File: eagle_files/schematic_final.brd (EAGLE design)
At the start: 77.9 x 100 mm, 46 parts, among them IC1 IC_ULN2003-TSSOP-16, T1 BPX81, T2 BPX81, T3 BPX81, T4 BPX81, T5 BPX81, T6 BPX81

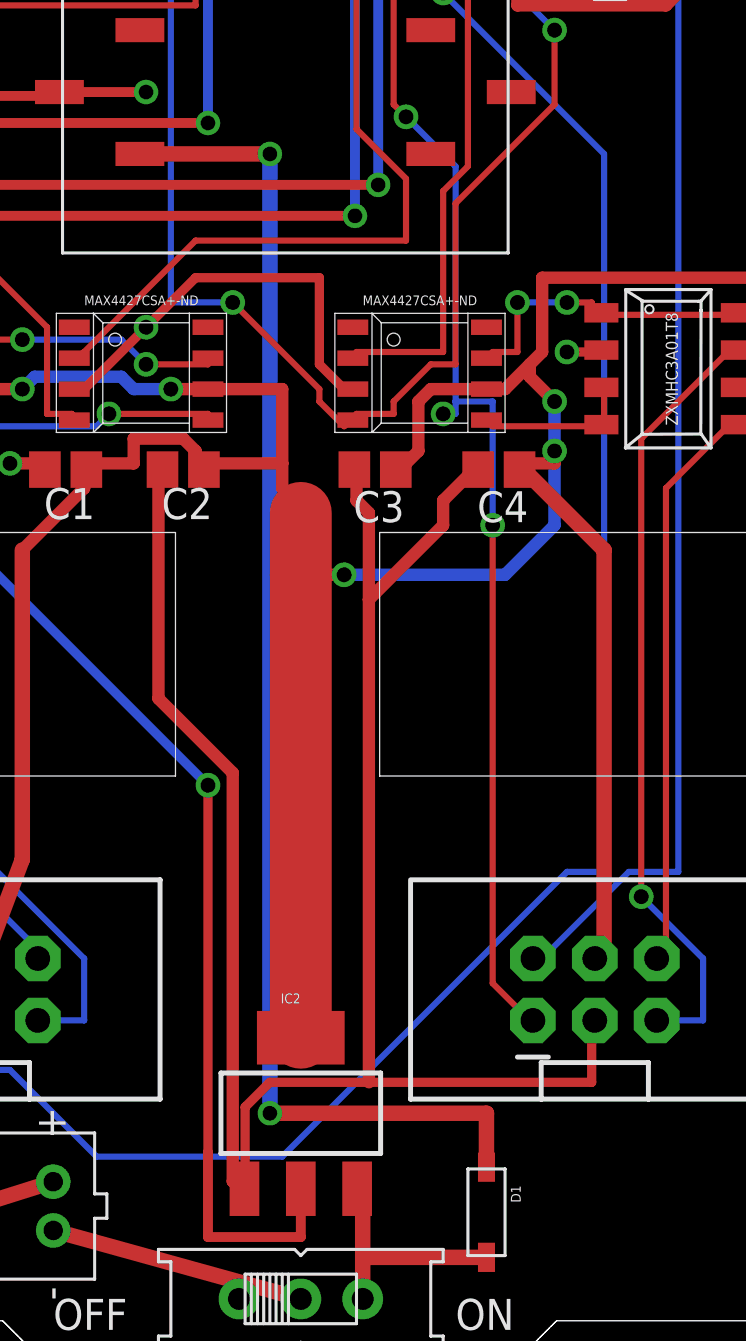
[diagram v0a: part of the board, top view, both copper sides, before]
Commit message: updated ground connections
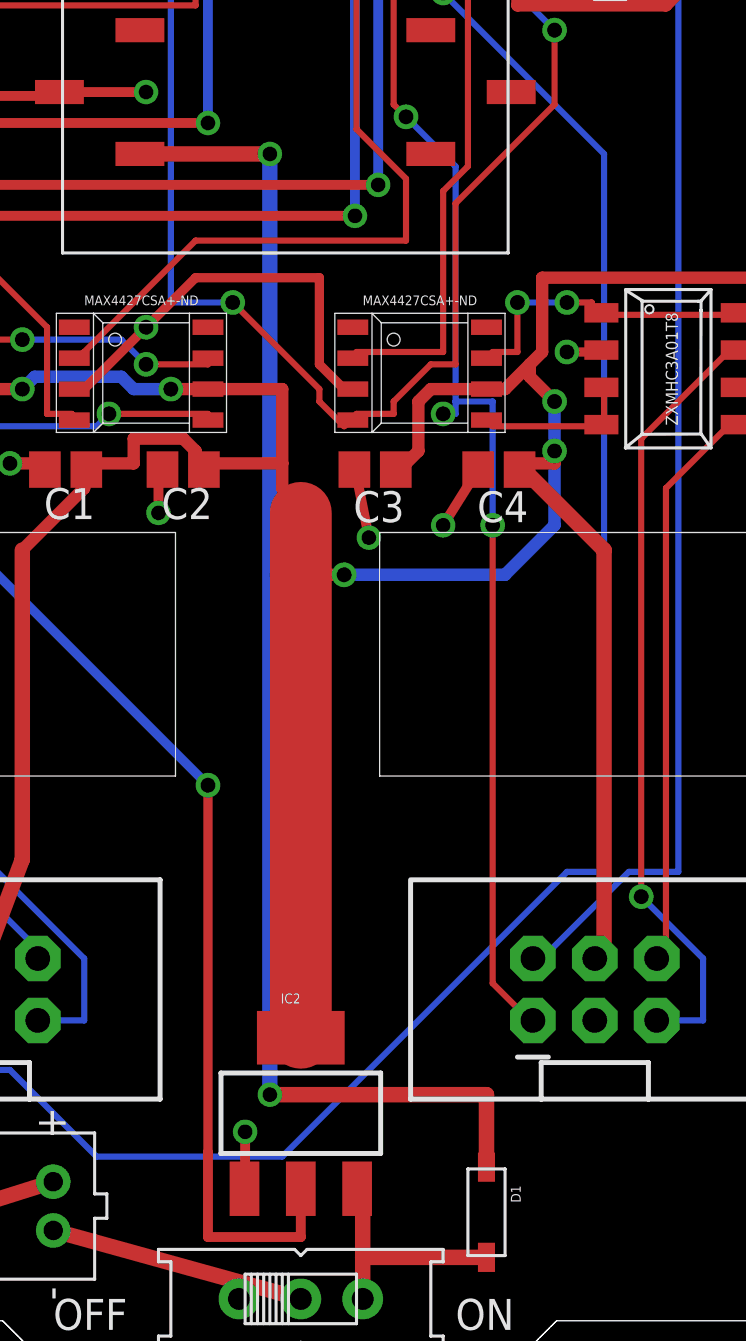
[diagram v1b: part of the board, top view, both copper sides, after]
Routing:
- net GND: track 163.5 -> 88.8 mm, vias 6 -> 10
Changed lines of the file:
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@@
 <wire x1="50.292" y1="42.672" x2="51.308" y2="42.672" width="0.381" layer="1"/>
 <wire x1="51.308" y1="42.672" x2="51.705" y2="42.75" width="0.381" layer="1"/>
-<wire x1="37.084" y1="11.684" x2="37.084" y2="8.636" width="0.381" layer="1"/>
-<wire x1="38.1" y1="12.7" x2="37.084" y2="11.684" width="0.381" layer="1"/>
-<wire x1="51.308" y1="12.7" x2="42.164" y2="12.7" width="0.381" layer="1"/>
-<wire x1="42.164" y1="12.7" x2="38.1" y2="12.7" width="0.381" layer="1"/>
-<wire x1="51.308" y1="15.24" x2="51.308" y2="12.7" width="0.381" layer="1"/>
 <wire x1="37.084" y1="8.636" x2="37.0586" y2="8.3312" width="0.381" layer="1"/>
-<wire x1="51.308" y1="15.24" x2="51.435" y2="15.24" width="0.381" layer="1"/>
 <via x="18.288" y="42.672" extent="1-16" drill="0.6096"/>
 <via x="50.292" y="42.672" extent="1-16" drill="0.6096"/>
@@
 <wire x1="27.432" y1="38.1" x2="28.448" y2="38.1" width="0.508" layer="1"/>
 <wire x1="28.448" y1="38.1" x2="28.868" y2="37.846" width="0.508" layer="1"/>
-<wire x1="33.528" y1="28.448" x2="33.528" y2="37.592" width="0.508" layer="1"/>
-<wire x1="36.576" y1="25.4" x2="33.528" y2="28.448" width="0.508" layer="1"/>
-<wire x1="36.576" y1="8.636" x2="36.576" y2="25.4" width="0.508" layer="1"/>
 <wire x1="33.528" y1="37.592" x2="33.694" y2="37.846" width="0.508" layer="1"/>
-<wire x1="36.576" y1="8.636" x2="37.0586" y2="8.3312" width="0.508" layer="1"/>
-<wire x1="41.656" y1="36.576" x2="41.656" y2="37.592" width="0.508" layer="1"/>
-<wire x1="42.164" y1="36.068" x2="41.656" y2="36.576" width="0.508" layer="1"/>
-<wire x1="42.164" y1="12.7" x2="42.164" y2="32.512" width="0.508" layer="1"/>
-<wire x1="42.164" y1="32.512" x2="42.164" y2="36.068" width="0.508" layer="1"/>
 <wire x1="41.656" y1="37.592" x2="41.568" y2="37.846" width="0.508" layer="1"/>
-<wire x1="45.212" y1="36.576" x2="46.228" y2="37.592" width="0.508" layer="1"/>
-<wire x1="45.212" y1="35.56" x2="45.212" y2="36.576" width="0.508" layer="1"/>
-<wire x1="42.164" y1="32.512" x2="45.212" y2="35.56" width="0.508" layer="1"/>
-<wire x1="46.228" y1="37.592" x2="46.648" y2="37.846" width="0.508" layer="1"/>
 <wire x1="50.8" y1="60.96" x2="48.26" y2="58.42" width="0.508" layer="1"/>
 <wire x1="52.07" y1="60.96" x2="50.8" y2="60.96" width="0.508" layer="1"/>
@@
 <via x="27.432" y="38.1" extent="1-16" drill="0.6096"/>
 <wire x1="40.132" y1="42.164" x2="40.132" y2="45.72" width="0.381" layer="1"/>
+<via x="42.164" y="35.052" extent="1-16" drill="0.6"/>
+<via x="45.212" y="35.56" extent="1-16" drill="0.6"/>
+<wire x1="41.656" y1="37.592" x2="42.164" y2="35.052" width="0.4064" layer="1"/>
+<wire x1="46.648" y1="37.846" x2="45.212" y2="35.56" width="0.4064" layer="1"/>
+<via x="33.528" y="36.068" extent="1-16" drill="0.6"/>
+<wire x1="33.528" y1="37.592" x2="33.528" y2="36.068" width="0.4064" layer="1"/>
+<wire x1="37.084" y1="8.636" x2="37.084" y2="10.668" width="0.4064" layer="1"/>
+<via x="37.084" y="10.668" extent="1-16" drill="0.6"/>
 </signal>
 <signal name="N$1">
@@
 <wire x1="32.766" y1="50.8" x2="38.1" y2="50.8" width="0.635" layer="1"/>
 <via x="38.1" y="50.8" extent="1-16" drill="0.6"/>
-<wire x1="38.1" y1="50.8" x2="38.1" y2="11.43" width="0.635" layer="16"/>
-<wire x1="46.99" y1="9.216" x2="46.99" y2="11.43" width="0.635" layer="1"/>
-<wire x1="46.99" y1="11.43" x2="38.1" y2="11.43" width="0.635" layer="1"/>
-<via x="38.1" y="11.43" extent="1-16" drill="0.6"/>
+<wire x1="38.1" y1="50.8" x2="38.1" y2="12.192" width="0.635" layer="16"/>
+<wire x1="46.99" y1="9.216" x2="46.99" y2="12.192" width="0.635" layer="1"/>
+<wire x1="46.99" y1="12.192" x2="38.1" y2="12.192" width="0.635" layer="1"/>
+<via x="38.1" y="12.192" extent="1-16" drill="0.6"/>
 </signal>
 <signal name="FRONT_R">

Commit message: updated board
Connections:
- removed net DIAG_L_IN: R12.2, T6.E
- removed net DIAG_R_IN: R11.2, T5.E
- removed net FRONT_L_IN: R6.2, T3.E
- removed net FRONT_R_IN: R5.2, T2.E
- removed net SIDE_L_IN: R8.2, T4.E
- removed net SIDE_R_IN: R7.2, T1.E
- net DIAG_L: now also R12.2, T6.E
- net DIAG_R: now also R11.2, T5.E
- net FRONT_L: now also R6.2, T3.E
- net FRONT_R: now also R5.2, T2.E
- net SIDE_L: now also R8.2, T4.E
- net SIDE_R: now also R7.2, T1.E
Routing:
- net SIDE_R: track 0.00 -> 155.2 mm, vias 0 -> 4
- net DIAG_R: track 0.00 -> 97.4 mm, vias 0 -> 5
- net SIDE_L: track 0.00 -> 58.0 mm, vias 0 -> 5
- net FRONT_R: track 0.00 -> 51.6 mm, vias 0 -> 1
- net DIAG_L: track 0.00 -> 35.9 mm, vias 0 -> 4
- net DIAG_R_IN: track 31.7 -> 0.00 mm, vias 1 -> 0
- net FRONT_L: track 0.00 -> 29.6 mm, vias 0 -> 2
- net L_ENC_B: track 116.6 -> 90.0 mm, vias 3 -> 2
- net FRONT_R_IN: track 25.3 -> 0.00 mm
- net SIDE_L_IN: track 22.6 -> 0.00 mm, vias 1 -> 0
- net FRONT_L_IN: track 18.9 -> 0.00 mm, vias 1 -> 0
- net SIDE_R_IN: track 15.6 -> 0.00 mm, vias 1 -> 0
- net DIAG_L_IN: track 11.8 -> 0.00 mm, vias 2 -> 0
- net IR_DIAG: track 48.9 -> 51.4 mm
- net N$6: track 10.5 -> 11.3 mm
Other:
- board text added: "1.2.0"
- board text added: "REV"
